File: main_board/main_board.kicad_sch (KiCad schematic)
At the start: 6 parts, among them J1 Conn_01x16, U1 Pico, U2 MPR121QR2

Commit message: Update main_board.kicad_sch
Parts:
- removed J1: Conn_01x16, symbol Connector_Generic:Conn_01x16
- added J13: Conn_01x16, Edge Connector:1.0mm Pitch Edge Connector 01x16, symbol Connector_Generic:Conn_01x16
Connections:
- net GND: now also U1.42 (GND), J13.1 (Pin_1), J13.16 (Pin_16)
- net PAD2: now reaches U2.10 (ELE2)
- net PAD2: now also J13.13 (Pin_13)
- net PAD3: now reaches U2.11 (ELE3)
- net PAD3: now also J13.12 (Pin_12)
- net PAD4: now reaches U2.12 (LED0/ELE4)
- net PAD4: now also J13.11 (Pin_11)
- net PAD5: now reaches U2.13 (LED1/ELE5)
- net PAD5: now also J13.10 (Pin_10)
- net PAD6: now reaches U2.14 (LED2/ELE6)
- net PAD6: now also J13.9 (Pin_9)
- net PAD7: now reaches U2.15 (LED3/ELE7)
- net PAD7: now also J13.8 (Pin_8)
- net PAD8: now reaches U2.16 (LED4/ELE8)
- net PAD8: now also J13.7 (Pin_7)
- net PAD9: now reaches U2.17 (LED5/ELE9)
- net PAD9: now also J13.6 (Pin_6)
- net PAD10: now reaches U2.18 (LED6/ELE10)
- net PAD10: now also J13.5 (Pin_5)
- net PAD11: now reaches U2.19 (LED7/ELE11)
- net PAD11: now also J13.4 (Pin_4)
- net PAD0: now reaches U2.8 (ELE0)
- net PAD0: now also J13.15 (Pin_15)
- net PAD1: now reaches U2.9 (ELE1)
- net PAD1: now also J13.14 (Pin_14)
- no-connect marks 0 -> 33

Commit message: Main board complete?
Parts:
- C1, C2: footprint (none) -> Capacitor_SMD:C_0805_2012Metric_Pad1.18x1.45mm_HandSolder
- J13: footprint Edge Connector:1.0mm Pitch Edge Connector 01x16 -> Connector_FFC-FPC:TE_1-84952-6_1x16-1MP_P1.0mm_Horizontal
- R1: footprint (none) -> Resistor_SMD:R_0805_2012Metric_Pad1.20x1.40mm_HandSolder
- U1: footprint RPi_Pico:RPi_Pico_SMD_TH -> MCU_RaspberryPi_and_Boards:RPi_Pico_SMD_TH
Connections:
- net GND: no longer U1.42 (GND)
- net SDA: now reaches U1.26 (GPIO20)
- net SDA: now also U2.3 (SDA)
- net SCL: now reaches U1.27 (GPIO21)
- net SCL: now also U2.2 (SCL)
- net GP6: no longer names the net of U1.9 (GPIO6)
- net GP6: no longer U2.3 (SDA)
- net GP7: no longer names the net of U1.10 (GPIO7)
- net GP7: no longer U2.2 (SCL)
- no-connect marks 33 -> 34
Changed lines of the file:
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@@
   (no_connect (at 136.525 86.36))
   (no_connect (at 100.965 86.36))
+  (no_connect (at 100.965 91.44))
   (no_connect (at 100.965 111.76))
   (no_connect (at 136.525 109.22))
-  (no_connect (at 136.525 104.14))
   (no_connect (at 100.965 109.22))
   (no_connect (at 136.525 93.98))
+  (no_connect (at 118.745 124.46))
   (no_connect (at 136.525 119.38))
   (no_connect (at 100.965 81.28))
-  (no_connect (at 136.525 106.68))
   (no_connect (at 100.965 99.06))
   (no_connect (at 136.525 111.76))
@@
   (no_connect (at 100.965 83.82))
   (no_connect (at 136.525 73.66))
+  (no_connect (at 100.965 93.98))
   (no_connect (at 100.965 96.52))
   (no_connect (at 170.815 51.435))
@@
     (stroke (width 0) (type default))
   )
-  (wire (pts (xy 136.525 101.6) (xy 140.335 101.6))
+  (wire (pts (xy 136.525 101.6) (xy 145.415 101.6))
     (stroke (width 0) (type default))
   )
@@
     (stroke (width 0) (type default))
   )
-  (wire (pts (xy 90.805 88.9) (xy 100.965 88.9))
+  (wire (pts (xy 97.155 88.9) (xy 100.965 88.9))
     (stroke (width 0) (type default))
   )
@@
     )
   )
-  (global_label "GP7" (shape input) (at 100.965 93.98 180) (fields_autoplaced)
-    (effects (font (size 1.27 1.27)) (justify right))
-    (property "Intersheetrefs" "${INTERSHEET_REFS}" (at 94.3097 93.98 0)
-      (effects (font (size 1.27 1.27)) (justify right) hide)
+  (global_label "SCL" (shape input) (at 136.525 104.14 0) (fields_autoplaced)
+    (effects (font (size 1.27 1.27)) (justify left))
+    (property "Intersheetrefs" "${INTERSHEET_REFS}" (at 142.9384 104.14 0)
+      (effects (font (size 1.27 1.27)) (justify left) hide)
     )
   )
@@
     )
   )
-  (global_label "GP6" (shape input) (at 174.625 86.36 180) (fields_autoplaced)
-    (effects (font (size 1.27 1.27)) (justify right))
-    (property "Intersheetrefs" "${INTERSHEET_REFS}" (at 167.9697 86.36 0)
+  (global_label "SDA" (shape input) (at 174.625 86.36 180) (fields_autoplaced)
+    (effects (font (size 1.27 1.27)) (justify right))
+    (property "Intersheetrefs" "${INTERSHEET_REFS}" (at 168.1511 86.36 0)
       (effects (font (size 1.27 1.27)) (justify right) hide)
     )
@@
     )
   )
-  (global_label "GP6" (shape input) (at 100.965 91.44 180) (fields_autoplaced)
-    (effects (font (size 1.27 1.27)) (justify right))
-    (property "Intersheetrefs" "${INTERSHEET_REFS}" (at 94.3097 91.44 0)
-      (effects (font (size 1.27 1.27)) (justify right) hide)
+  (global_label "SDA" (shape input) (at 136.525 106.68 0) (fields_autoplaced)
+    (effects (font (size 1.27 1.27)) (justify left))
+    (property "Intersheetrefs" "${INTERSHEET_REFS}" (at 142.9989 106.68 0)
+      (effects (font (size 1.27 1.27)) (justify left) hide)
     )
   )
@@
     )
   )
-  (global_label "GP7" (shape input) (at 174.625 88.9 180) (fields_autoplaced)
-    (effects (font (size 1.27 1.27)) (justify right))
-    (property "Intersheetrefs" "${INTERSHEET_REFS}" (at 167.9697 88.9 0)
+  (global_label "SCL" (shape input) (at 174.625 88.9 180) (fields_autoplaced)
+    (effects (font (size 1.27 1.27)) (justify right))
+    (property "Intersheetrefs" "${INTERSHEET_REFS}" (at 168.2116 88.9 0)
       (effects (font (size 1.27 1.27)) (justify right) hide)
     )
@@
     )
   )
-  (symbol (lib_id "power:GND") (at 140.335 101.6 0) (unit 1)
-    (in_bom yes) (on_board yes) (dnp no) (fields_autoplaced)
-    (property "Reference" "#PWR07" (at 140.335 107.95 0)
-      (effects (font (size 1.27 1.27)) hide)
-    )
-    (property "Value" "GND" (at 140.335 106.68 0)
-      (effects (font (size 1.27 1.27)))
-    )
-    (property "Footprint" "" (at 140.335 101.6 0)
-      (effects (font (size 1.27 1.27)) hide)
-    )
-    (property "Datasheet" "" (at 140.335 101.6 0)
+  (symbol (lib_id "power:GND") (at 145.415 101.6 0) (unit 1)
+    (in_bom yes) (on_board yes) (dnp no) (fields_autoplaced)
+    (property "Reference" "#PWR07" (at 145.415 107.95 0)
+      (effects (font (size 1.27 1.27)) hide)
+    )
+    (property "Value" "GND" (at 145.415 106.68 0)
+      (effects (font (size 1.27 1.27)))
+    )
+    (property "Footprint" "" (at 145.415 101.6 0)
+      (effects (font (size 1.27 1.27)) hide)
+    )
+    (property "Datasheet" "" (at 145.415 101.6 0)
       (effects (font (size 1.27 1.27)) hide)
     )
@@
       (effects (font (size 1.27 1.27)))
     )
-    (property "Footprint" "" (at 180.975 76.835 0)
+    (property "Footprint" "Capacitor_SMD:C_0805_2012Metric_Pad1.18x1.45mm_HandSolder" (at 180.975 76.835 0)
       (effects (font (size 1.27 1.27)) hide)
     )
@@
         (path "/4a11fb4e-37e4-46fa-b38a-c052d00a21bc"
           (reference "C1") (unit 1)
-        )
-      )
-    )
-  )
-  (symbol (lib_id "power:GND") (at 118.745 124.46 0) (unit 1)
-    (in_bom yes) (on_board yes) (dnp no) (fields_autoplaced)
-    (property "Reference" "#PWR016" (at 118.745 130.81 0)
-      (effects (font (size 1.27 1.27)) hide)
-    )
-    (property "Value" "GND" (at 118.745 129.54 0)
-      (effects (font (size 1.27 1.27)))
-    )
-    (property "Footprint" "" (at 118.745 124.46 0)
-      (effects (font (size 1.27 1.27)) hide)
-    )
-    (property "Datasheet" "" (at 118.745 124.46 0)
-      (effects (font (size 1.27 1.27)) hide)
-    )
-    (pin "1")
-    (instances
-      (project "main_board"
-        (path "/4a11fb4e-37e4-46fa-b38a-c052d00a21bc"
-          (reference "#PWR016") (unit 1)
         )
       )
@@
     )
   )
-  (symbol (lib_id "power:GND") (at 90.805 88.9 0) (unit 1)
-    (in_bom yes) (on_board yes) (dnp no) (fields_autoplaced)
-    (property "Reference" "#PWR010" (at 90.805 95.25 0)
-      (effects (font (size 1.27 1.27)) hide)
-    )
-    (property "Value" "GND" (at 90.805 93.98 0)
-      (effects (font (size 1.27 1.27)))
-    )
-    (property "Footprint" "" (at 90.805 88.9 0)
-      (effects (font (size 1.27 1.27)) hide)
-    )
-    (property "Datasheet" "" (at 90.805 88.9 0)
+  (symbol (lib_id "power:GND") (at 97.155 88.9 0) (unit 1)
+    (in_bom yes) (on_board yes) (dnp no) (fields_autoplaced)
+    (property "Reference" "#PWR010" (at 97.155 95.25 0)
+      (effects (font (size 1.27 1.27)) hide)
+    )
+    (property "Value" "GND" (at 97.155 93.98 0)
+      (effects (font (size 1.27 1.27)))
+    )
+    (property "Footprint" "" (at 97.155 88.9 0)
+      (effects (font (size 1.27 1.27)) hide)
+    )
+    (property "Datasheet" "" (at 97.155 88.9 0)
       (effects (font (size 1.27 1.27)) hide)
     )
@@
       (effects (font (size 1.27 1.27)))
     )
-    (property "Footprint" "RPi_Pico:RPi_Pico_SMD_TH" (at 118.745 95.25 90)
+    (property "Footprint" "MCU_RaspberryPi_and_Boards:RPi_Pico_SMD_TH" (at 118.745 95.25 90)
       (effects (font (size 1.27 1.27)) hide)
     )
@@
       (effects (font (size 1.27 1.27)))
     )
-    (property "Footprint" "" (at 169.545 109.22 0)
+    (property "Footprint" "Capacitor_SMD:C_0805_2012Metric_Pad1.18x1.45mm_HandSolder" (at 169.545 109.22 0)
       (effects (font (size 1.27 1.27)) hide)
     )
@@
       (effects (font (size 1.27 1.27)))
     )
-    (property "Footprint" "" (at 169.545 104.14 0)
+    (property "Footprint" "Resistor_SMD:R_0805_2012Metric_Pad1.20x1.40mm_HandSolder" (at 169.545 104.14 0)
       (effects (font (size 1.27 1.27)) hide)
     )
@@
       (effects (font (size 1.27 1.27)))
     )
-    (property "Footprint" "Edge Connector:1.0mm Pitch Edge Connector 01x16" (at 183.515 46.355 0)
-      (effects (font (size 1.27 1.27)) hide)
-    )
+    (property "Footprint" "Connector_FFC-FPC:TE_1-84952-6_1x16-1MP_P1.0mm_Horizontal" (at 183.515 46.355 0)
+      (effects (font (size 1.27 1.27)) hide)
+    )

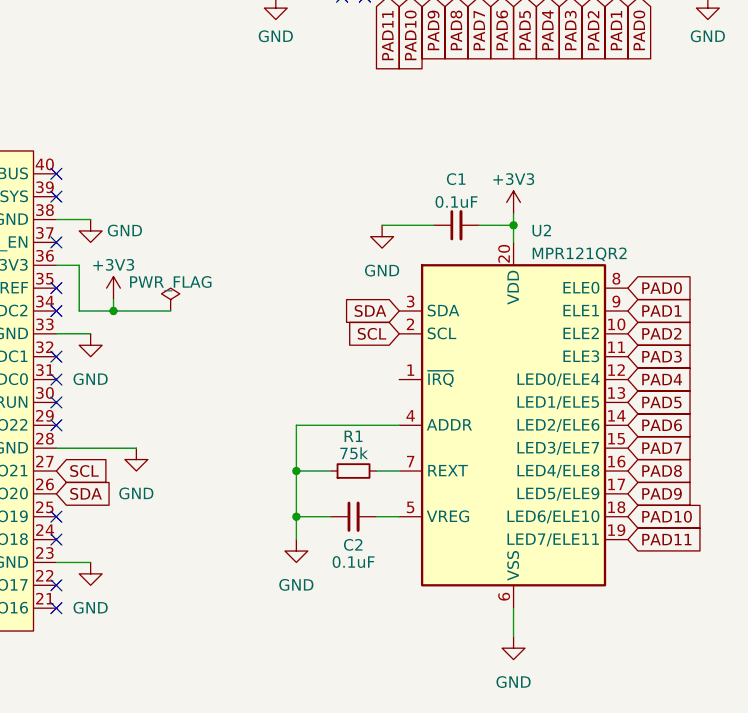
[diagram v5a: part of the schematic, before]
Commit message: Add tooling holes, update logo, other adjustments
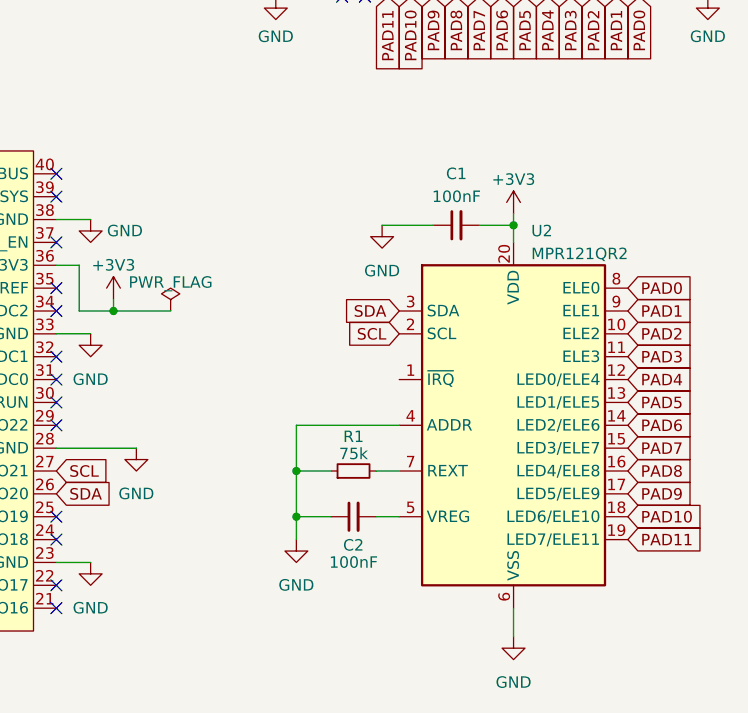
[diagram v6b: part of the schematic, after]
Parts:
- C1, C2: value 0.1uF -> 100nF; LCSC (none) -> C49678
- R1: LCSC (none) -> C17819
- U2: LCSC (none) -> C91322
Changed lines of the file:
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@@
   (symbol (lib_id "Device:C_Small") (at 180.975 76.835 90) (unit 1)
     (in_bom yes) (on_board yes) (dnp no) (fields_autoplaced)
-    (property "Reference" "C1" (at 180.9813 71.755 90)
-      (effects (font (size 1.27 1.27)))
-    )
-    (property "Value" "0.1uF" (at 180.9813 74.295 90)
+    (property "Reference" "C1" (at 180.9813 71.12 90)
+      (effects (font (size 1.27 1.27)))
+    )
+    (property "Value" "100nF" (at 180.9813 73.66 90)
       (effects (font (size 1.27 1.27)))
     )
@@
     )
     (property "Datasheet" "~" (at 180.975 76.835 0)
+      (effects (font (size 1.27 1.27)) hide)
+    )
+    (property "LCSC" "C49678" (at 180.975 76.835 0)
       (effects (font (size 1.27 1.27)) hide)
     )
@@
     )
     (property "Datasheet" "" (at 118.745 95.25 0)
+      (effects (font (size 1.27 1.27)) hide)
+    )
+    (property "LCSC" "" (at 118.745 95.25 0)
       (effects (font (size 1.27 1.27)) hide)
     )
@@
       (effects (font (size 1.27 1.27)))
     )
-    (property "Value" "0.1uF" (at 169.545 114.3 90)
+    (property "Value" "100nF" (at 169.545 114.3 90)
       (effects (font (size 1.27 1.27)))
     )
@@
     )
     (property "Datasheet" "~" (at 169.545 109.22 0)
+      (effects (font (size 1.27 1.27)) hide)
+    )
+    (property "LCSC" "C49678" (at 169.545 109.22 0)
       (effects (font (size 1.27 1.27)) hide)
     )
@@
     )
     (property "Datasheet" "https://resurgentsemi.com/wp-content/uploads/2018/09/MPR121_rev5-Resurgent.pdf?d453f8&d453f8" (at 175.895 106.68 0)
+      (effects (font (size 1.27 1.27)) hide)
+    )
+    (property "LCSC" "C91322" (at 187.325 99.06 0)
       (effects (font (size 1.27 1.27)) hide)
     )
@@
       (effects (font (size 1.27 1.27)) hide)
     )
+    (property "LCSC" "C17819" (at 169.545 104.14 0)
+      (effects (font (size 1.27 1.27)) hide)
+    )
     (pin "1")
     (pin "2")
@@
       (effects (font (size 1.27 1.27)) hide)
     )
+    (property "LCSC" "" (at 183.515 46.355 0)
+      (effects (font (size 1.27 1.27)) hide)
+    )
